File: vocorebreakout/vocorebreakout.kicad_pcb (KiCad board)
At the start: 2 copper layers, 75 x 87.3 mm, 53 parts, among them J1 8P8C_LED_Shielded, J10 Top, J11 Right, J12 Conn_02x04_Odd_Even, J2 8P8C_LED_Shielded, J3 8P8C_LED_Shielded, J4 Conn_01x03, J5 Left, J6 Bottom, J7 Conn_02x04_Top_Bottom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

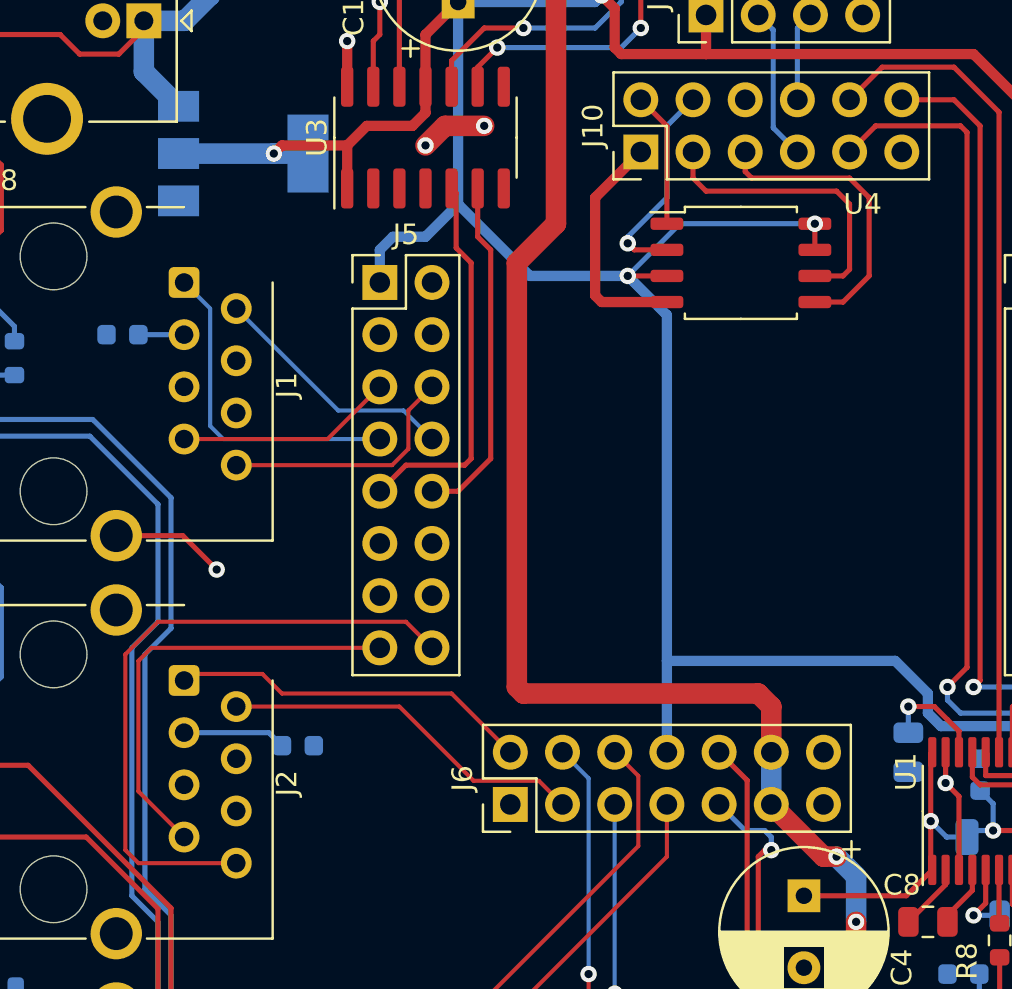
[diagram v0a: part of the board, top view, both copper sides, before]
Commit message: vocorebreakout: Move SPI flash to bottom and ethernet port to #2
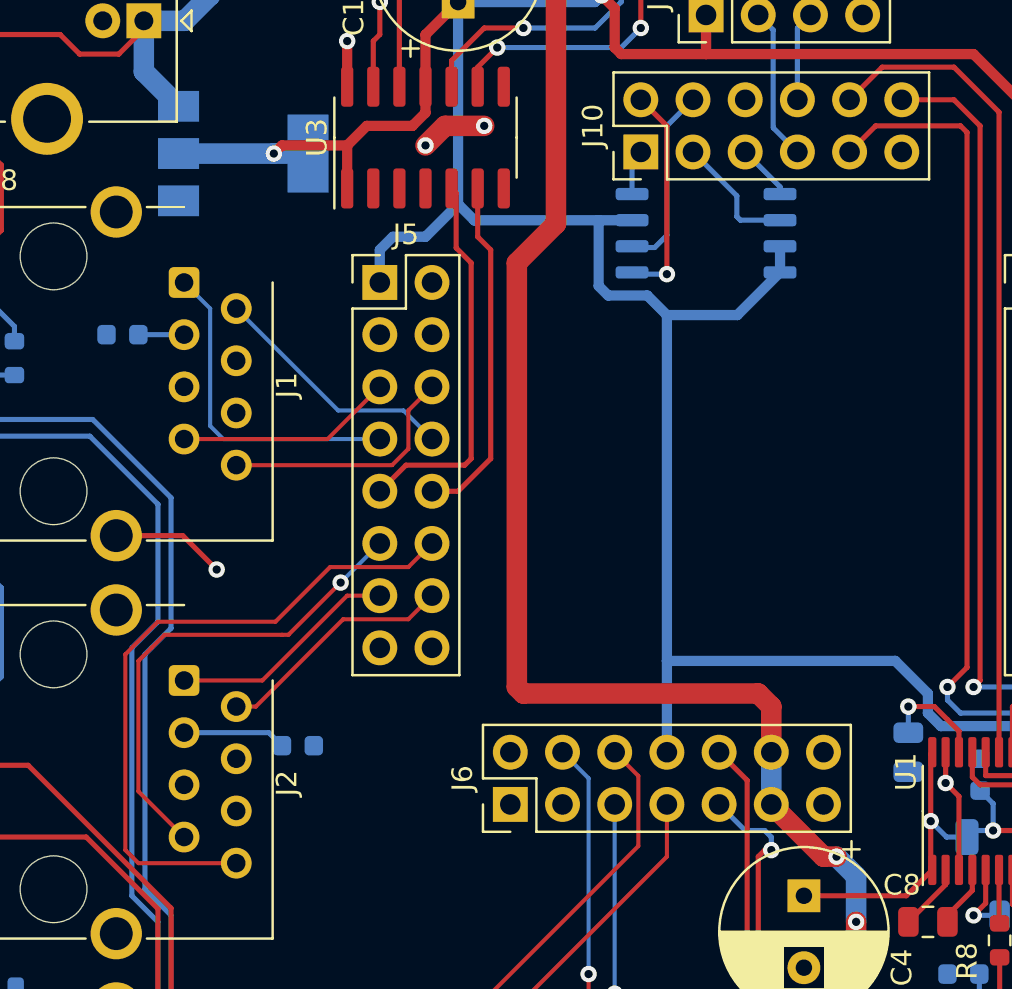
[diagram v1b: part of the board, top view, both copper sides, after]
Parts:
- U4: moved to B.Cu
- moved U4 2.23 mm to (88.9, 73.8)
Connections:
- J5 pad 11: unconnected-(J5-Pad11) -> /RD2+
- J5 pad 12: unconnected-(J5-Pad12) -> /RD2-
- J5 pad 13: unconnected-(J5-Pad13) -> /TD2+
- J5 pad 14: unconnected-(J5-Pad14) -> /TD2-
- J5 pad 15: /RD2+ -> unconnected-(J5-Pad15)
- J5 pad 16: /RD2- -> unconnected-(J5-Pad16)
- J6 pad 2: /TD2+ -> unconnected-(J6-Pad2)
- J6 pad 3: /TD2- -> unconnected-(J6-Pad3)
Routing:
- net /SPI_MOSI: track 14.5 -> 2.75 mm
- net GND: track 55.1 -> 45.8 mm
- net /SPI_CLK: track 14.4 -> 6.20 mm
- net /TD2-: track 17.8 -> 11.8 mm
- net /TD2+: track 17.6 -> 11.7 mm
- net /SPI_CS: track 6.56 -> 10.7 mm, vias 0 -> 1
- net +3.3V: track 182.3 -> 180.1 mm, vias 5 -> 3
- net /RD2+: track 21.5 -> 23.6 mm, vias 0 -> 1
- net /SPI_MISO: track 10.3 -> 9.09 mm, vias 1 -> 0
- net /RD2-: track 31.3 -> 32.3 mm
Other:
- board text added: "website.peterjin.org /wiki/VoCore2_Breakout Rev 2 2024-03-10"
- board text removed: "website.peterjin.org /wiki/VoCore2_Breakout Rev 1 2024-02-17"
